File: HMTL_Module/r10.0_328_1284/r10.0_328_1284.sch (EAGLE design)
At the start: 39 parts, among them J2 AVR_SPI_PRG_6PTH, Y1 20MHz

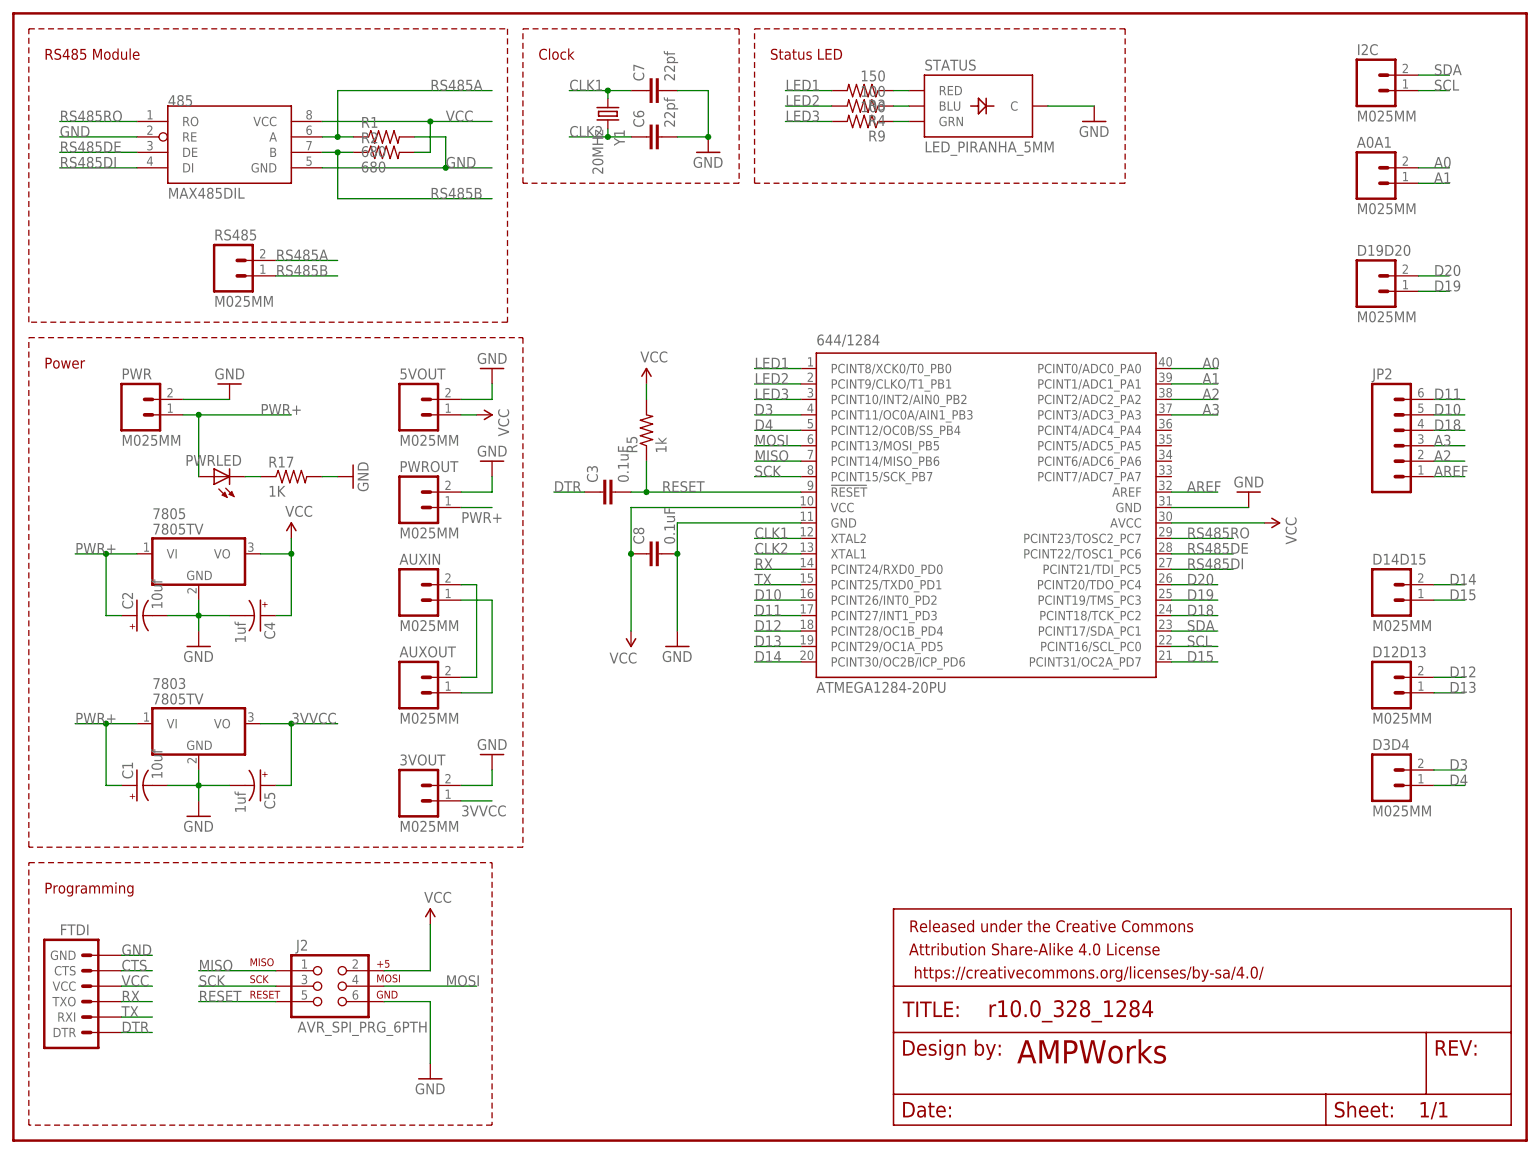
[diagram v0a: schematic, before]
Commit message: Added correct 328 plus 1284 layout based on most recent 1284 layout
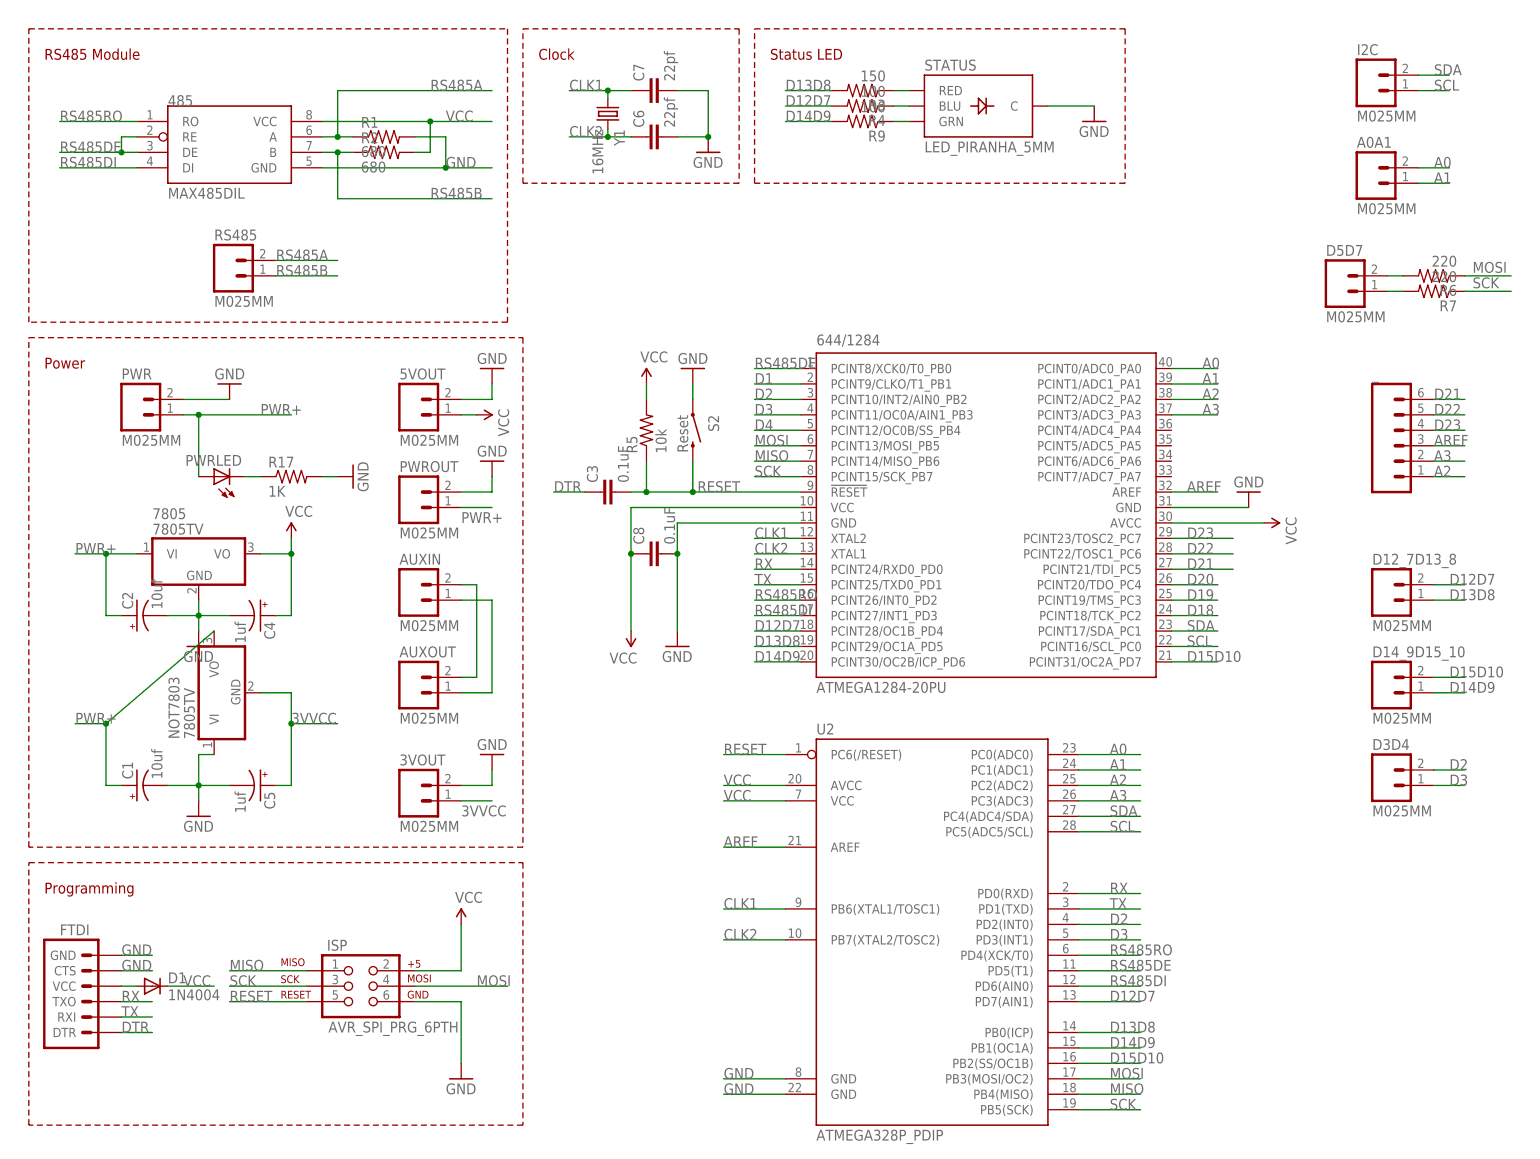
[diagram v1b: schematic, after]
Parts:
- removed 7803: 7805TV, linear:7805TV
- removed D19D20: M025MM, SparkFun-Connectors:M025MM
- removed FRAME1: FRAME-LETTER, SparkFun-Aesthetics:FRAME-LETTER
- removed J2: AVR_SPI_PRG_6PTH, SparkFun-Connectors:AVR_SPI_PRG_6PTH
- added D1: 1N4004, adafruit:1N4004
- added D5D7: M025MM, SparkFun-Connectors:M025MM
- added ISP: AVR_SPI_PRG_6PTH, SparkFun-Connectors:AVR_SPI_PRG_6PTH
- added NOT7803: 7805TV, linear:7805TV
- added R6, R7: 220, SparkFun-Passives:RESISTORPTH-1/4W
- added S2: Reset, SparkFun:SWITCH-MOMENTARY-2SMD
- added U2: ATMEGA328P_PDIP, SparkFun-DigitalIC:ATMEGA328P_PDIP
- R5: value 1k -> 10k
- Y1: value 20MHz -> 16MHz
- renumbered D12D13 to D14_9D15_10, D14D15 to D12_7D13_8, JP2 to _
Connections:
- removed net CTS: FTDI.CTS
- removed net D10: 644/1284.PCINT26/INT0_PD2, _.5
- removed net D11: 644/1284.PCINT27/INT1_PD3, _.6
- removed net D12: 644/1284.PCINT28/OC1B_PD4, D14_9D15_10.2
- removed net D13: 644/1284.PCINT29/OC1A_PD5, D14_9D15_10.1
- removed net D14: 644/1284.PCINT30/OC2B/ICP_PD6, D12_7D13_8.2
- removed net D15: 644/1284.PCINT31/OC2A_PD7, D12_7D13_8.1
- removed net LED1: 644/1284.PCINT8/XCK0/T0_PB0, R3.2
- removed net LED2: 644/1284.PCINT9/CLKO/T1_PB1, R4.2
- removed net LED3: 644/1284.PCINT10/INT2/AIN0_PB2, R9.2
- new net D1: 644/1284.PCINT9/CLKO/T1_PB1
- new net D12D7: 644/1284.PCINT28/OC1B_PD4, D12_7D13_8.2, R4.2, U2.PD7(AIN1)
- new net D13D8: 644/1284.PCINT29/OC1A_PD5, D12_7D13_8.1, R3.2, U2.PB0(ICP)
- new net D14D9: 644/1284.PCINT30/OC2B/ICP_PD6, D14_9D15_10.1, R9.2, U2.PB1(OC1A)
- new net D15D10: 644/1284.PCINT31/OC2A_PD7, D14_9D15_10.2, U2.PB2(SS/OC1B)
- new net D2: 644/1284.PCINT10/INT2/AIN0_PB2, D3D4.2, U2.PD2(INT0)
- new net D21: 644/1284.PCINT21/TDI_PC5, _.6
- new net D22: 644/1284.PCINT22/TOSC1_PC6, _.5
- new net D23: 644/1284.PCINT23/TOSC2_PC7, _.4
- new net N$4: D5D7.2, R6.2
- new net N$8: D5D7.1, R7.2
- new net N$9: D1.A, FTDI.VCC
- net 3VVCC: now also NOT7803.GND; no longer 7803.VO
- net A0: now also U2.PC0(ADC0)
- net A1: now also U2.PC1(ADC1)
- net A2: now also U2.PC2(ADC2), _.1; no longer _.2
- net A3: now also U2.PC3(ADC3), _.2; no longer _.3
- net AREF: now also U2.AREF, _.3; no longer _.1
- net CLK1: now also U2.PB6(XTAL1/TOSC1)
- net CLK2: now also U2.PB7(XTAL2/TOSC2)
- net D18: no longer _.4
- net D19: no longer D19D20.1
- net D20: no longer D19D20.2
- net D3: now also D3D4.1, U2.PD3(INT1); no longer D3D4.2
- net D4: no longer D3D4.1
- net GND: now also FTDI.CTS, ISP.6, NOT7803.VI, S2.1, U2.GND@1, U2.GND@2; no longer 485.RE, 7803.GND, J2.6
- net MISO: now also ISP.1, U2.PB4(MISO); no longer J2.1
- net MOSI: now also ISP.4, R6.1, U2.PB3(MOSI/OC2); no longer J2.4
- net PWR+: now also NOT7803.VO; no longer 7803.VI
- net RESET: now also ISP.5, S2.2, U2.PC6(/RESET); no longer J2.5
- net RS485DE: now also 485.RE, 644/1284.PCINT8/XCK0/T0_PB0, U2.PD5(T1); no longer 644/1284.PCINT22/TOSC1_PC6
- net RS485DI: now also 644/1284.PCINT27/INT1_PD3, U2.PD6(AIN0); no longer 644/1284.PCINT21/TDI_PC5
- net RS485RO: now also 644/1284.PCINT26/INT0_PD2, U2.PD4(XCK/T0); no longer 644/1284.PCINT23/TOSC2_PC7
- net RX: now also U2.PD0(RXD)
- net SCK: now also ISP.3, R7.1, U2.PB5(SCK); no longer J2.3
- net SCL: now also U2.PC5(ADC5/SCL)
- net SDA: now also U2.PC4(ADC4/SDA)
- net TX: now also U2.PD1(TXD)
- net VCC: now also D1.C, ISP.2, U2.AVCC, U2.VCC; no longer FTDI.VCC, J2.2
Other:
- note removed: "AMPWorks"
